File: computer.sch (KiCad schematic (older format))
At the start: 18 parts, among them J1 Expansion, J2 Expansion, SW1 RESET, U4 74HC00, U5 DS1813, X1 1MHz

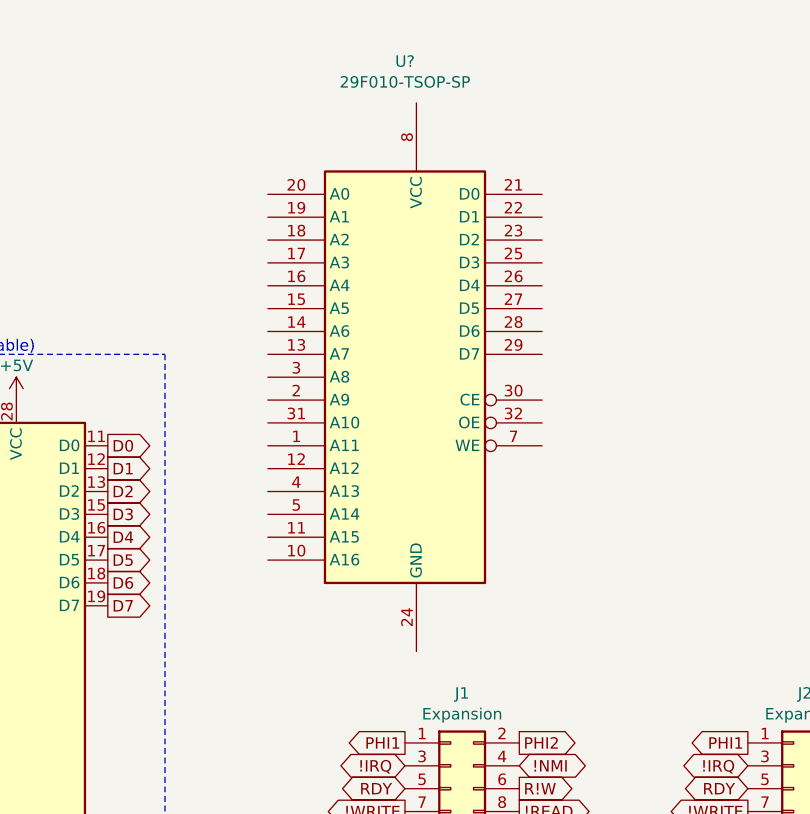
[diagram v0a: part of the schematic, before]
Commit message: Remove not yet required IC from schematic
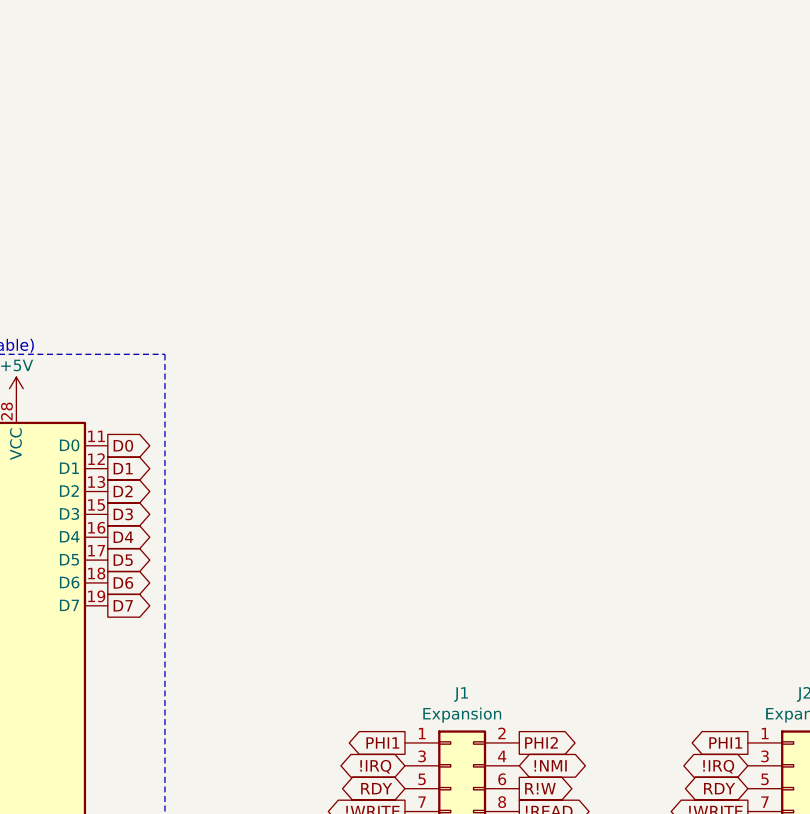
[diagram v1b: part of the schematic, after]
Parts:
- removed U?: 29F010-TSOP-SP, symbol Memory_Flash:29F010-TSOP-SP
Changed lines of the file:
@@
-	1    0    0    -1
-$EndComp
-$Comp
-L Memory_Flash:29F010-TSOP-SP U?
-U 1 1 5FC3DC27
-P 8200 2150
-F 0 "U?" H 8200 3531 50  0000 C CNN
-F 1 "29F010-TSOP-SP" H 8200 3440 50  0000 C CNN
-F 2 "" H 8200 2150 50  0001 C CNN
-F 3 "" H 8200 2150 50  0001 C CNN
-	1    8200 2150
 	1    0    0    -1
 $EndComp

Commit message: Tidying
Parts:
- renumbered CPU to U1, ROM to U2, RAM to U3
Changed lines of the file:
@@
 A0
 $Comp
-L Memory_RAM:CY62256-70PC RAM
+L Memory_RAM:CY62256-70PC U3
 U 1 1 5FAF655C
 P 1650 4500
-F 0 "RAM" H 1700 3550 50  0000 L CNN
+F 0 "U3" H 1700 3550 50  0000 L CNN
 F 1 "AS6C62256" H 1700 3650 50  0000 L CNN
 F 2 "Package_DIP:DIP-28_W15.24mm_Socket" H 1650 4400 50  0001 C CNN
@@
 Connection ~ 3550 3450
 $Comp
-L 65xx:W65C02SxP CPU
+L 65xx:W65C02SxP U1
 U 1 1 5FAC057B
 P 4400 3800
-F 0 "CPU" H 4450 2300 50  0000 L CNN
+F 0 "U1" H 4450 2300 50  0000 L CNN
 F 1 "W65C02SxP" H 4450 2400 50  0000 L CIB
 F 2 "Package_DIP:DIP-40_W15.24mm_Socket" H 4400 5800 50  0001 C CNN
@@
 $EndComp
 $Comp
-L Memory_EEPROM:28C256 ROM
+L Memory_EEPROM:28C256 U2
 U 1 1 5FAF9279
 P 6500 3350
-F 0 "ROM" H 6550 2200 50  0000 L CNN
+F 0 "U2" H 6550 2200 50  0000 L CNN
 F 1 "28C256" H 6550 2300 50  0000 L CNN
 F 2 "Package_DIP:DIP-28_W15.24mm_Socket" H 6500 3350 50  0001 C CNN

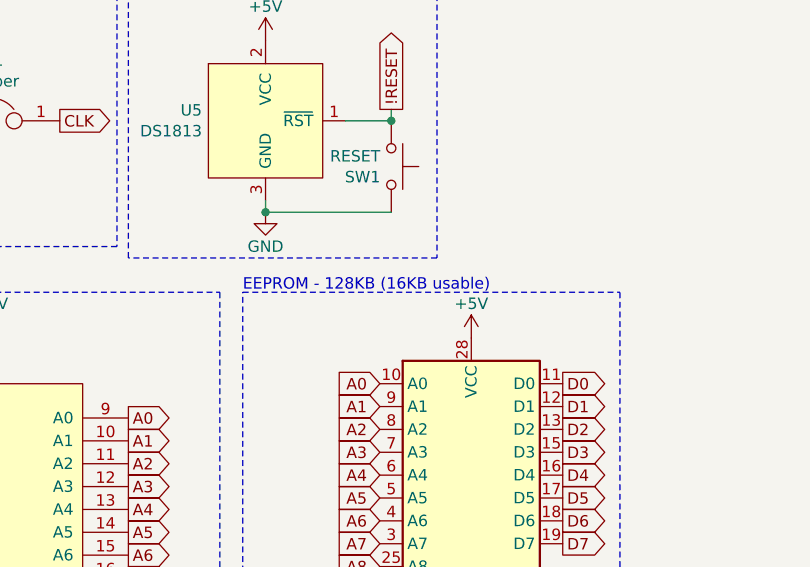
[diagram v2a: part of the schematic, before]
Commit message: Fix EEPROM description
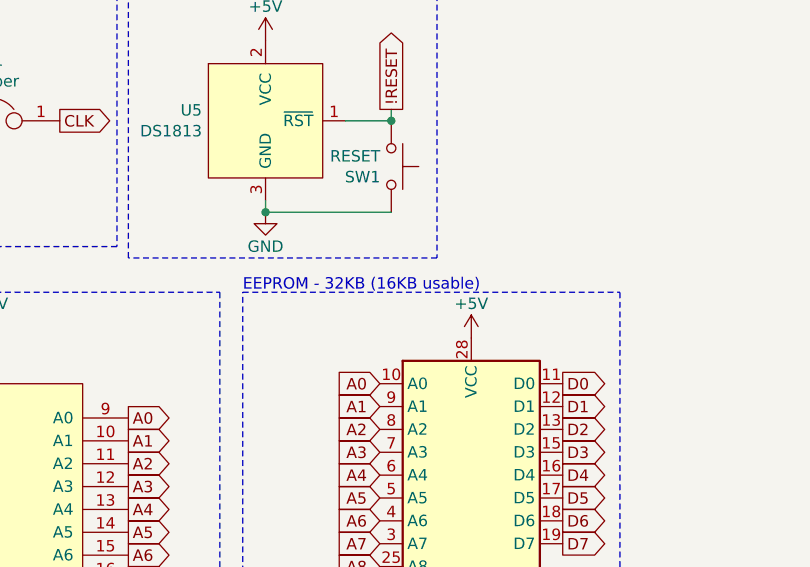
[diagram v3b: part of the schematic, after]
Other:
- note added: "EEPROM - 32KB (16KB usable)"
- note removed: "EEPROM - 128KB (16KB usable)"
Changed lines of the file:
@@
 Just a 6502.
 Text Notes 5500 2050 0    50   ~ 0
-EEPROM - 128KB (16KB usable)
+EEPROM - 32KB (16KB usable)
 Wire Notes Line
 	5500 2050 7150 2050

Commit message: Tidy schematic
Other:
- note removed: "Notes:\n\nThere are several peripherals still to do: serial, storage, keyboard, audio.\nThere are no decoupling caps, or power supplies for 74xx yet.\nThe video card is not quite complete. It requires the HSYNC/VSYNC to be set up.\nThe video card may or may not actually work. This is a first draft.\n\nSorry there are not wires. I like labels."
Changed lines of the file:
@@
 EELAYER 30 0
 EELAYER END
-$Descr A3 16535 11693
+$Descr A4 11693 8268
 encoding utf-8
 Sheet 1 1
@@
 	1    0    0    -1
 $EndComp
-Text Notes 1150 10950 0    79   ~ 0
-Notes:\n\nThere are several peripherals still to do: serial, storage, keyboard, audio.\nThere are no decoupling caps, or power supplies for 74xx yet.\nThe video card is not quite complete. It requires the HSYNC/VSYNC to be set up.\nThe video card may or may not actually work. This is a first draft.\n\nSorry there are not wires. I like labels.
 Text GLabel 5000 2600 2    50   Output ~ 0
 A0

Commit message: More tidying up
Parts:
- C1, C2, C3, C4: footprint Capacitor_THT:C_Rect_L7.2mm_W2.5mm_P5.00mm_FKS2_FKP2_MKS2_MKP2 -> Capacitor_THT:C_Disc_D6.0mm_W2.5mm_P5.00mm
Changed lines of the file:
@@
 Text GLabel 8700 4050 2    50   Output ~ 0
 !READ
-Text GLabel 4700 1300 2    50   Output ~ 0
-CLK
 Text GLabel 8200 4150 0    50   BiDi ~ 0
 CLK
@@
 F 0 "C4" H 7000 5250 50  0000 L CNN
 F 1 "0.1uF" H 6900 5150 50  0000 L CNN
-F 2 "Capacitor_THT:C_Rect_L7.2mm_W2.5mm_P5.00mm_FKS2_FKP2_MKS2_MKP2" H 7238 5050 50  0001 C CNN
+F 2 "Capacitor_THT:C_Disc_D6.0mm_W2.5mm_P5.00mm" H 7238 5050 50  0001 C CNN
 F 3 "~" H 7200 5200 50  0001 C CNN
 	1    7200 5200
@@
 F 0 "C3" H 6550 5250 50  0000 L CNN
 F 1 "0.1uF" H 6450 5150 50  0000 L CNN
-F 2 "Capacitor_THT:C_Rect_L7.2mm_W2.5mm_P5.00mm_FKS2_FKP2_MKS2_MKP2" H 6788 5050 50  0001 C CNN
+F 2 "Capacitor_THT:C_Disc_D6.0mm_W2.5mm_P5.00mm" H 6788 5050 50  0001 C CNN
 F 3 "~" H 6750 5200 50  0001 C CNN
 	1    6750 5200
@@
 F 0 "C2" H 6100 5250 50  0000 L CNN
 F 1 "0.1uF" H 6000 5150 50  0000 L CNN
-F 2 "Capacitor_THT:C_Rect_L7.2mm_W2.5mm_P5.00mm_FKS2_FKP2_MKS2_MKP2" H 6338 5050 50  0001 C CNN
+F 2 "Capacitor_THT:C_Disc_D6.0mm_W2.5mm_P5.00mm" H 6338 5050 50  0001 C CNN
 F 3 "~" H 6300 5200 50  0001 C CNN
 	1    6300 5200
@@
 F 0 "C1" H 5650 5250 50  0000 L CNN
 F 1 "0.1uF" H 5550 5150 50  0000 L CNN
-F 2 "Capacitor_THT:C_Rect_L7.2mm_W2.5mm_P5.00mm_FKS2_FKP2_MKS2_MKP2" H 5888 5050 50  0001 C CNN
+F 2 "Capacitor_THT:C_Disc_D6.0mm_W2.5mm_P5.00mm" H 5888 5050 50  0001 C CNN
 F 3 "~" H 5850 5200 50  0001 C CNN
 	1    5850 5200
 	1    0    0    -1
 $EndComp
+Text GLabel 4700 1300 2    50   Output ~ 0
+CLK
 $EndSCHEMATC
